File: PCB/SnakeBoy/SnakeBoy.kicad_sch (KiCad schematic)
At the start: 15 parts, among them SW1 X, SW2 A, SW3 Y, SW4 B, SW5 Start, SW6 Select, SW7 SW_DIP_x01, U1 ESP32-S3-DEVKITC-1-N16R8, U2 Joystick, U3 PAM8304 Module, U4 TP4056 Module

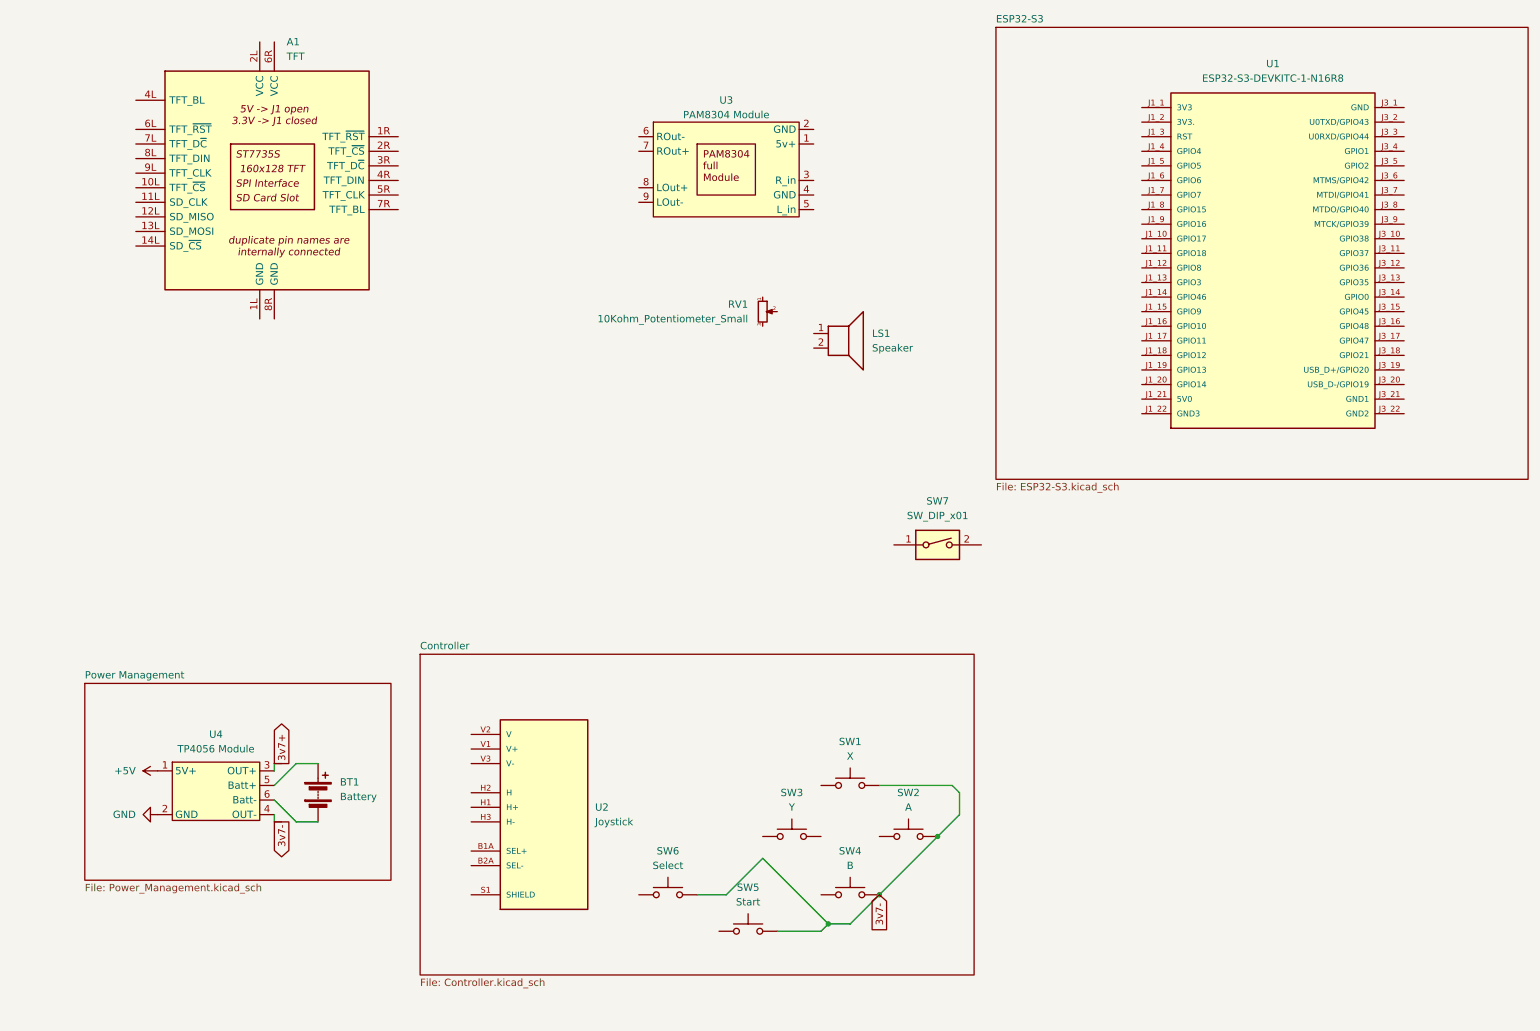
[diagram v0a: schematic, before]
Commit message: Finished the Controller and Display schems
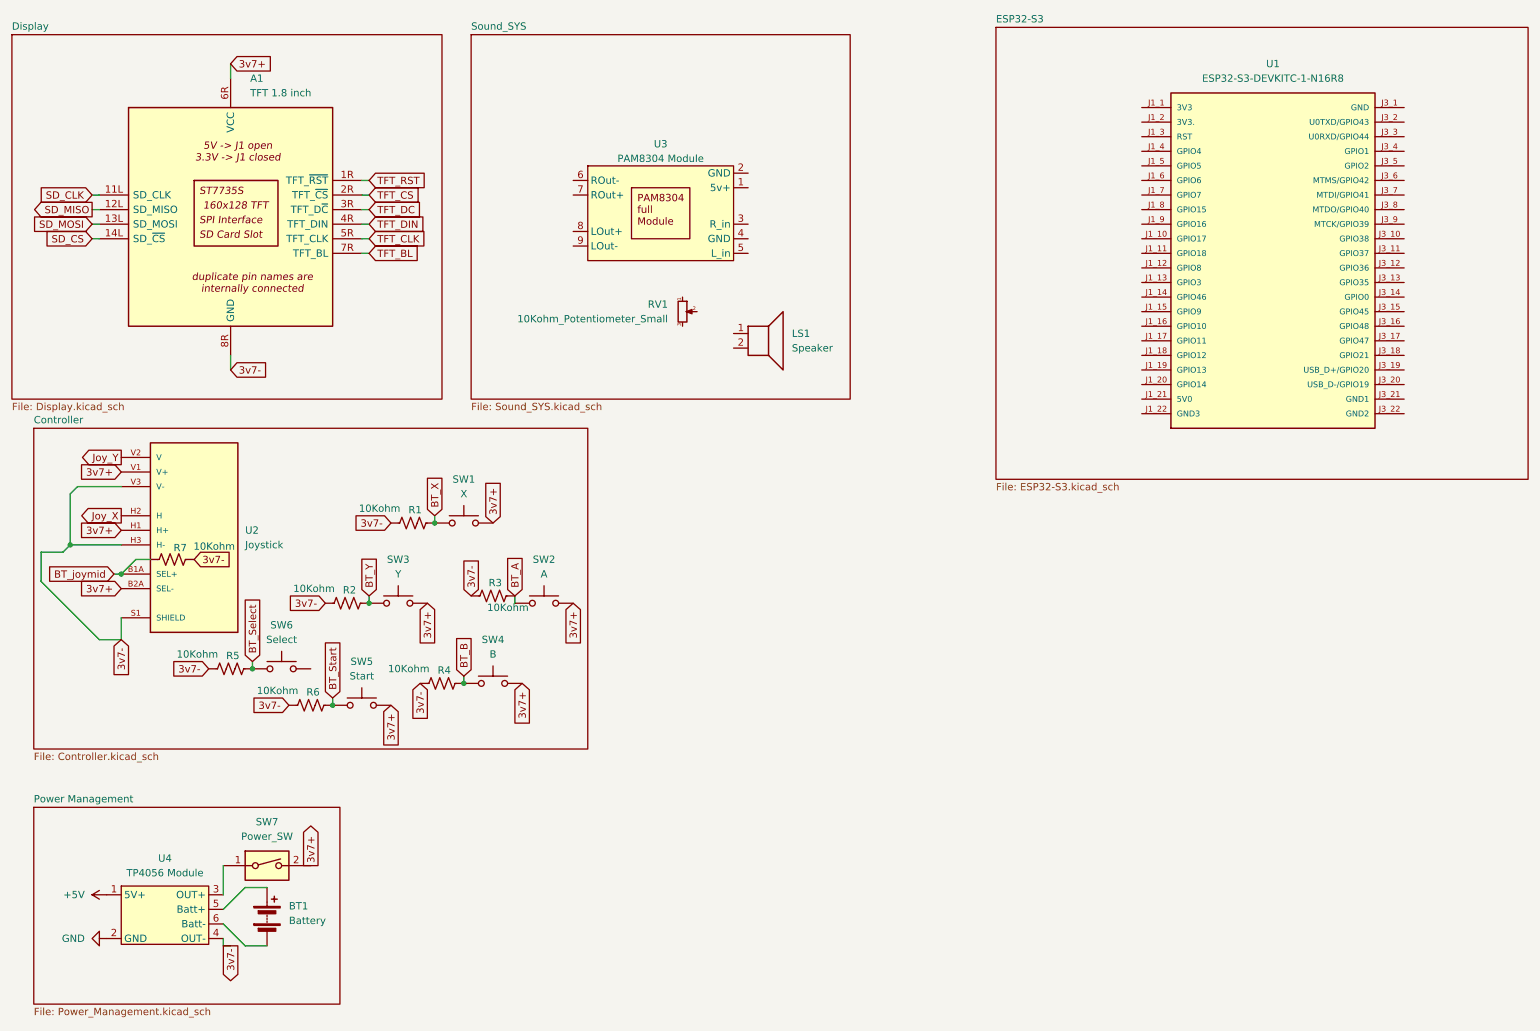
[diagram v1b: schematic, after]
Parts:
- added R1, R2, R3, R4, R5, R6, R7: 10Kohm, symbol Device:R_US
- A1: value TFT -> TFT 1.8 inch
- SW7: value SW_DIP_x01 -> Power_SW
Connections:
- net 3v7+: now also A1.6R (VCC), SW1.2, SW2.2, SW3.2, SW4.2, SW5.2, SW7.2, U2.B2A (SEL-), U2.H1 (H+), U2.V1 (V+); no longer U4.3 (OUT+)
- net 3v7-: now also A1.8R (GND), U2.H3 (H-), U2.S1 (SHIELD), U2.S2 (SHIELD), U2.S3 (SHIELD), U2.S4 (SHIELD), U2.V3 (V-), R1.2, R2.2, R3.2, R4.2, R5.2, R6.2, R7.2; no longer SW1.2, SW2.2, SW4.2, SW5.2, SW6.2
- net BT_B: now reaches SW4.1
- net BT_B: now also R4.1
- net at SW7.1: now also U4.3 (OUT+)
- net BT_X: now reaches SW1.1
- net BT_X: now also R1.1
- net BT_Y: now reaches SW3.1
- net BT_Y: now also R2.1
- net BT_Select: now reaches SW6.1
- net BT_Select: now also R5.1
- net BT_A: now reaches SW2.1
- net BT_A: now also R3.1
- net BT_Start: now reaches SW5.1
- net BT_Start: now also R6.1
- net SD_CLK: now reaches A1.11L (SD_CLK)
- net SD_MISO: now reaches A1.12L (SD_MISO)
- net SD_MOSI: now reaches A1.13L (SD_MOSI)
- net SD_CS: now reaches A1.14L (SD_~{CS})
- net TFT_RST: now reaches A1.1R (TFT_~{RST})
- net TFT_CS: now reaches A1.2R (TFT_~{CS})
- net TFT_DC: now reaches A1.3R (TFT_D~{C})
- net TFT_DIN: now reaches A1.4R (TFT_DIN)
- net TFT_CLK: now reaches A1.5R (TFT_CLK)
- net TFT_BL: now reaches A1.7R (TFT_BL)
- net BT_joymid: now reaches U2.B1A (SEL+)
- net BT_joymid: now also R7.1
- net Joy_X: now reaches U2.H2 (H)
- net Joy_Y: now reaches U2.V2 (V)
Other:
- added sheet Display (Display.kicad_sch)
- added sheet Sound_SYS (Sound_SYS.kicad_sch)
- moved on the sheet: BT1, LS1, RV1, SW1, SW2, SW3, SW4, SW5, SW6, SW7, U2, U3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

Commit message: Finished the schematic
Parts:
- added LS2: Speaker_L, Connector_JST:JST_XH_S2B-XH-A-1_1x02_P2.50mm_Horizontal, symbol Device:Speaker
- LS1: value Speaker -> Speaker_R
- R1, R2, R3, R4, R5, R6, R7: footprint (none) -> Resistor_THT:R_Axial_DIN0309_L9.0mm_D3.2mm_P12.70mm_Horizontal
- RV1: value 10Kohm_Potentiometer_Small -> Pot_Dual; footprint slider:RA2043F2010EB1B10K -> slider:PS45M0MC2BR10KN; symbol Device:R_Potentiometer_Small -> Device:R_Potentiometer_Dual
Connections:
- net 3v7+: now also U1.J1_21 (5V0), U3.1 (5v+); no longer A1.6R (VCC), SW1.2, SW2.2, SW3.2, SW4.2, SW5.2, U2.B2A (SEL-), U2.H1 (H+), U2.V1 (V+)
- net 3v7-: now also RV1.A1, RV1.B1, U1.J3_1 (GND), U3.2 (GND), U3.4 (GND)
- net BT_A: now also U1.J3_3 (U0RXD/GPIO44)
- net BT_B: now also U1.J3_18 (GPIO21)
- net BT_Select: now also U1.J3_16 (GPIO48)
- net BT_Start: now also U1.J3_15 (GPIO45)
- net BT_X: now also U1.J3_10 (GPIO38)
- net BT_Y: now also U1.J3_2 (U0TXD/GPIO43)
- net BT_joymid: now also U1.J3_17 (GPIO47)
- net Joy_X: now also U1.J1_16 (GPIO10)
- net Joy_Y: now also U1.J1_15 (GPIO9)
- net SD_CLK: now also U1.J3_7 (MTDI/GPIO41)
- net SD_CS: now also U1.J1_17 (GPIO11)
- net SD_MISO: now also U1.J3_6 (MTMS/GPIO42)
- net SD_MOSI: now also U1.J1_12 (GPIO8)
- net TFT_BL: now also U1.J1_4 (GPIO4)
- net TFT_CLK: now also U1.J1_5 (GPIO5)
- net TFT_CS: now also U1.J3_9 (MTCK/GPIO39)
- net TFT_DC: now also U1.J1_7 (GPIO7)
- net TFT_DIN: now also U1.J1_6 (GPIO6)
- net TFT_RST: now also U1.J3_8 (MTDO/GPIO40)
- net ROut-: now reaches LS1.1
- net ROut-: now also U3.6 (ROut-)
- net ROut+ vol: now reaches LS1.2
- net ROut+ vol: now also RV1.B3
- net 3v3+: now reaches SW6.2
- net 3v3+: now also A1.6R (VCC), SW1.2, SW2.2, SW3.2, SW4.2, SW5.2, U1.J1_1 (3V3), U2.B2A (SEL-), U2.H1 (H+), U2.V1 (V+)
- net R_in: now reaches U3.3 (R_in)
- net R_in: now also U1.J3_4 (GPIO1)
- net L_in: now reaches U3.5 (L_in)
- net L_in: now also U1.J3_5 (GPIO2)
- net ROut+: now reaches U3.7 (ROut+)
- net ROut+: now also RV1.B2
- net LOut+: now reaches U3.8 (LOut+)
- net LOut+: now also RV1.A2
- net LOut-: now reaches U3.9 (LOut-)
- net LOut-: now also LS2.1
- new net LOut+ vol: LS2.2, RV1.A3
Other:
- moved on the sheet: LS1, U1, U3
